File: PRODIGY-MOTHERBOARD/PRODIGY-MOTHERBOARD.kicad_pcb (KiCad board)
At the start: 2 copper layers, 217 parts, among them J1 USB_A, J10 CAN, J11 SERIAL, J12 MOTOR, J13 MOTOR, J15 Barrel_Jack_MountingPin, J16 AudioJack3, J19 KEYPAD_MATRIX, J2 SERVO, J20 Ultrasonic, J21 GPIO, J22 GPIO, J23 GPIO, J24 12V OUT, J3 SERVO, J4 SERVO, J5 GPIO, J6 DM3BT-DSF-PEJS/C, J7 A_OUT, J8 SPI_OUT, J9 I2C, P2 USB_C_Plug, Q1 BC850, Q2 BS870, Q3 BC850, Q4 DMP2045U-7, Q5 BC850, SW1 SW_SPST, SW2 SW_SPST, SW3 SW_SPST, SW4 SW_SPST, U1 PN5321A3HN_C1xx, U10 DRV8870DDA, U11 CR2013-MI2120, U12 PCF8574, U13 SN74LVC1T45DBV, U15 CC56-12YWA, U16 LM386, U17 TXS0108EPW, U18 PCA9306DC, U19 PCF8574, U2 SN74LVC1T45DBV, U20 LIS2DH12TR, U21 DRV8870DDA, U22 IP4252CZ16, U23 MCP6021RT-E/OT, U24 TSDP341xx, U3 TPS22810DRV, U4 TPS54331DR, U5 TPS54331DR, U6 Si4460, U7 LM386, U8 HDC1080, U9 SN65HVD232

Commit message: CAN schematic done
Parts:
- removed C1: 4.7uF, Capacitor_SMD:C_1206_3216Metric
- removed C32: 1uF, Capacitor_SMD:C_0603_1608Metric
- removed C33: 100nF, Capacitor_SMD:C_0603_1608Metric
- removed C34: 100nF C0G, Capacitor_SMD:C_1206_3216Metric
- removed C35: 47uF, Capacitor_SMD:C_1210_3225Metric
- removed C36, C38: 10uF, Capacitor_SMD:C_1206_3216Metric
- removed the D1 at (41.6, 119.7)
- removed the D1 at (117.3, 125.7)
- removed the D10 at (19.0, 134.4)
- removed the D10 at (158.5, 135.4)
- removed the D11 at (158.5, 142.0)
- removed the D11 at (19.0, 141.0)
- removed the D12 at (33.5, 121.7)
- removed the D12 at (166.9, 115.5)
- removed the D13 at (33.5, 129.2)
- removed the D13 at (166.9, 122.2)
- removed the D14 at (166.9, 128.8)
- removed the D14 at (19.0, 147.7)
- removed the D15 at (173.6, 116.0)
- removed the D15 at (27.4, 121.2)
- removed the D16 at (27.4, 127.8)
- removed the D16 at (181.1, 116.0)
- removed the D17 at (188.6, 116.0)
- removed the D17 at (27.4, 134.4)
- removed the D2 at (17.2, 114.1)
- removed the D2 at (117.3, 136.8)
- removed the D21 at (153.7, 55.5)
- removed the D21 at (173.0, 131.1)
- removed D25, D27: SD05_SOD323, Diode_SMD:D_SOD-323
- removed the D3 at (24.7, 114.1)
- removed the D3 at (117.3, 131.2)
- removed the D4 at (32.2, 114.1)
- removed the D4 at (139.5, 84.0)
- removed the D5 at (102.5, 56.9)
- removed the D5 at (19.0, 121.2)
- removed the D6 at (181.1, 129.1)
- removed the D6 at (39.7, 114.1)
- removed the D7 at (158.5, 115.5)
- removed the D7 at (47.2, 114.1)
- removed the D8 at (54.7, 114.1)
- removed the D8 at (158.5, 122.2)
- removed the D9 at (19.0, 127.8)
- removed the D9 at (158.5, 128.8)
- removed J1: USB_A, Connector_USB:USB_A_TE_292303-7_Horizontal
- removed the J12 at (126.2, 51.8)
- removed the J12 at (89.2, 83.5)
- removed J2, J3: SERVO, Connector_JST:JST_XH_S3B-XH-A_1x03_P2.50mm_Horizontal
- removed the J4 at (169.7, 69.0)
- removed the J4 at (101.2, 70.0)
- removed P2: USB_C_Plug, Connector_USB:USB_C_Receptacle_GCT_USB4105-xx-A_16P_TopMnt_Horizontal
- removed the Q1 at (49.1, 119.7)
- removed the Q1 at (188.6, 129.1)
- removed the Q3 at (144.2, 47.0)
- removed the Q3 at (207.8, 97.1)
- removed R25: 100, Resistor_SMD:R_0805_2012Metric
- removed R26, R27, R28: 220k, Resistor_SMD:R_0805_2012Metric
- removed R29: 1k, Resistor_SMD:R_0805_2012Metric
- removed RN5: 10k, Resistor_SMD:R_Array_Convex_5x0603
- removed SW1, SW2, SW3, SW4: SW_SPST, Button_Switch_SMD:SW_SPST_EVQP0
- removed U1: PN5321A3HN_C1xx, Package_DFN_QFN:HVQFN-40-1EP_6x6mm_P0.5mm_EP4.1x4.1mm
- removed U10: DRV8870DDA, Package_SO:Texas_HTSOP-8-1EP_3.9x4.9mm_P1.27mm_EP2.95x4.9mm_Mask2.4x3.1mm_ThermalVias
- added C25: 47uF, Capacitor_SMD:C_1210_3225Metric, F.Cu at (132.8, 29.6)
- added C26: 47uF, Capacitor_SMD:C_1210_3225Metric, F.Cu at (132.8, 33.8)
- added C27: 47uF, Capacitor_SMD:C_1210_3225Metric, F.Cu at (132.8, 38.1)
- added C28: 47uF, Capacitor_SMD:CP_Elec_6.3x5.8, F.Cu at (145.0, 155.5)
- added C29: 47uF, Capacitor_SMD:CP_Elec_6.3x5.8, F.Cu at (145.0, 163.6)
- added C40: 100nF, Capacitor_SMD:C_0603_1608Metric, F.Cu at (83.2, 145.2)
- added C41: 100nF C0G, Capacitor_SMD:C_1206_3216Metric, F.Cu at (77.9, 150.6)
- added C42: 47uF, Capacitor_SMD:C_1210_3225Metric, F.Cu at (77.9, 157.8)
- added C43: 10uF, Capacitor_SMD:C_1206_3216Metric, F.Cu at (77.9, 154.0)
- added C58: 100nF, Capacitor_SMD:C_0603_1608Metric, F.Cu at (85.7, 64.5)
- added D1: D_Schottky, Diode_SMD:D_SMB, F.Cu at (148.0, 142.2)
- added D10: LED, LED_THT:LED_D5.0mm, F.Cu at (110.3, 146.2)
- added D11: LED, LED_THT:LED_D5.0mm, F.Cu at (117.8, 146.2)
- added D12: LED, LED_THT:LED_D5.0mm, F.Cu at (125.3, 146.2)
- added D13: WS2812B, LED_SMD:LED_WS2812B_PLCC4_5.0x5.0mm_P3.2mm, F.Cu at (95.2, 128.2)
- added D14: D_IR_EMITTER, LED_THT:LED_D5.0mm_Horizontal_O1.27mm_Z3.0mm_Clear, F.Cu at (126.8, 159.3)
- added D15: WS2812B, LED_SMD:LED_WS2812B_PLCC4_5.0x5.0mm_P3.2mm, F.Cu at (95.2, 134.8)
- added D16: WS2812B, LED_SMD:LED_WS2812B_PLCC4_5.0x5.0mm_P3.2mm, F.Cu at (95.2, 141.4)
- added D17: WS2812B, LED_SMD:LED_WS2812B_PLCC4_5.0x5.0mm_P3.2mm, F.Cu at (95.2, 148.0)
- added D2: SD05_SOD323, Diode_SMD:D_SOD-323, F.Cu at (154.3, 140.8)
- added D21: LED, LED_THT:LED_D5.0mm, F.Cu at (117.8, 153.8)
- added D22: WS2812B, LED_SMD:LED_WS2812B_PLCC4_5.0x5.0mm_P3.2mm, F.Cu at (103.6, 128.2)
- added D29: SD05_SOD323, Diode_SMD:D_SOD-323, F.Cu at (83.0, 71.3)
- added D3: SD05_SOD323, Diode_SMD:D_SOD-323, F.Cu at (154.3, 143.8)
- added D30: SD05_SOD323, Diode_SMD:D_SOD-323, F.Cu at (83.0, 74.2)
- added D4: D_Schottky, Diode_SMD:D_SMB, F.Cu at (161.6, 21.7)
- added D5: D_Schottky, Diode_SMD:D_SMB, F.Cu at (161.6, 27.3)
- added D6: D_Schottky, Diode_SMD:D_SMB, F.Cu at (161.6, 32.8)
- added D7: D_Schottky, Diode_SMD:D_SMB, F.Cu at (154.4, 72.8)
- added D8: SD05_SOD323, Diode_SMD:D_SOD-323, F.Cu at (82.9, 150.4)
- added D9: SD05_SOD323, Diode_SMD:D_SOD-323, F.Cu at (82.9, 153.4)
- added J12: I2C, Connector_JST:JST_XH_S4B-XH-A_1x04_P2.50mm_Horizontal, F.Cu at (22.7, 84.5)
- added J14: SERIAL, Connector_JST:JST_XH_S4B-XH-A_1x04_P2.50mm_Horizontal, F.Cu at (22.7, 111.7)
- added J17: SERVO, Connector_JST:JST_XH_S3B-XH-A_1x03_P2.50mm_Horizontal, F.Cu at (68.5, 111.7)
- added J18: SERVO, Connector_JST:JST_XH_S3B-XH-A_1x03_P2.50mm_Horizontal, F.Cu at (80.5, 111.7)
- added J26: KEYPAD_MATRIX, Connector_PinHeader_2.54mm:PinHeader_1x08_P2.54mm_Vertical_SMD_Pin1Left, F.Cu at (23.2, 68.0)
- added J4: USB_A, Connector_USB:USB_A_TE_292303-7_Horizontal, F.Cu at (62.2, 130.8)
- added L3: L_Iron_Coupled_1324, Inductor_SMD:L_CommonModeChoke_TDK_ACM7060, F.Cu at (92.0, 72.5)
- added P1: USB_C_Plug, Connector_USB:USB_C_Receptacle_GCT_USB4105-xx-A_16P_TopMnt_Horizontal, F.Cu at (156.1, 65.3)
- added Q1: DMP2045U-7, Package_TO_SOT_SMD:SOT-23, F.Cu at (65.5, 159.6)
- added Q3: BC850, Package_TO_SOT_SMD:SOT-23, F.Cu at (126.3, 127.3)
- added R18: 1k 1%, Resistor_SMD:R_0603_1608Metric, F.Cu at (145.7, 35.3)
- added R19: 10k 1%, Resistor_SMD:R_0603_1608Metric, F.Cu at (149.7, 20.2)
- added R20: 1k 1%, Resistor_SMD:R_0603_1608Metric, F.Cu at (149.7, 22.7)
- added R21: 680 1%, Resistor_SMD:R_0603_1608Metric, F.Cu at (149.7, 25.2)
- added R63: 100, Resistor_SMD:R_0603_1608Metric, F.Cu at (121.8, 133.7)
- added R64: R_Photo, OptoDevice:R_LDR_5.1x4.3mm_P3.4mm_Vertical, F.Cu at (37.4, 160.8)
- added R65: 10k, Resistor_SMD:R_0603_1608Metric, F.Cu at (91.7, 64.5)
- added R66: 100, Resistor_SMD:R_0603_1608Metric, F.Cu at (91.7, 67.0)
- added R67: 59, Resistor_SMD:R_1206_3216Metric, F.Cu at (78.0, 71.5)
- added R68: 59, Resistor_SMD:R_1206_3216Metric, F.Cu at (78.0, 74.8)
- added RN4: 4.7k, Resistor_SMD:R_Array_Convex_4x0603, F.Cu at (33.4, 67.5)
- added U14: SN74LVC1T45DBV, Package_TO_SOT_SMD:SOT-23-6, F.Cu at (164.5, 97.5)
- added U25: TJA1051T-E, Package_SO:SOIC-8_3.9x4.9mm_P1.27mm, F.Cu at (79.4, 66.6)
- C10: value 100nF -> 4.7uF; footprint Capacitor_SMD:C_0603_1608Metric -> Capacitor_SMD:C_1206_3216Metric
- C11, C12: value 10nF -> 4.7uF; footprint Capacitor_SMD:C_0603_1608Metric -> Capacitor_SMD:C_1206_3216Metric
- C13: value 1nF -> 4.7uF; footprint Capacitor_SMD:C_0603_1608Metric -> Capacitor_SMD:C_1206_3216Metric
- C14: value 4.7nF -> 100nF
- C15: value 47pF -> 100nF
- C16: value 39pF -> 10nF
- C17: value 100nF -> 10nF
- C18: value 100nF -> 1nF
- C19: value 47uF -> 4.7nF; footprint Capacitor_SMD:C_1210_3225Metric -> Capacitor_SMD:C_0603_1608Metric
- C2: value 22nF -> 10uF; footprint Capacitor_SMD:C_0603_1608Metric -> Capacitor_SMD:C_0805_2012Metric
- C20: value 47uF -> 47pF; footprint Capacitor_SMD:C_1210_3225Metric -> Capacitor_SMD:C_0603_1608Metric
- C21: value 47uF -> 39pF; footprint Capacitor_SMD:C_1210_3225Metric -> Capacitor_SMD:C_0603_1608Metric
- C22: value 47uF -> 100nF; footprint Capacitor_SMD:C_1210_3225Metric -> Capacitor_SMD:C_0603_1608Metric
- C23: value 10uF -> 100nF; footprint Capacitor_SMD:C_0805_2012Metric -> Capacitor_SMD:C_0603_1608Metric
- C24, C9: value 100nF -> 47uF; footprint Capacitor_SMD:C_0603_1608Metric -> Capacitor_SMD:C_1210_3225Metric
- C3: value 100uF -> 100nF; footprint Capacitor_SMD:CP_Elec_6.3x7.7 -> Capacitor_SMD:C_0603_1608Metric
- C39: value 100nF -> 1uF; footprint Capacitor_SMD:C_0805_2012Metric -> Capacitor_SMD:C_0603_1608Metric
- C4: value 47uF -> 10uF; footprint Capacitor_SMD:C_1210_3225Metric -> Capacitor_SMD:C_1206_3216Metric
- C5: value 4.7uF -> 100nF; footprint Capacitor_SMD:C_1206_3216Metric -> Capacitor_SMD:C_0805_2012Metric
- C7: value 4.7uF -> 22nF; footprint Capacitor_SMD:C_1206_3216Metric -> Capacitor_SMD:C_0603_1608Metric
- C8: value 4.7uF -> 100uF; footprint Capacitor_SMD:C_1206_3216Metric -> Capacitor_SMD:CP_Elec_6.3x7.7
- D18, D23: value LED -> WS2812B; footprint LED_THT:LED_D5.0mm -> LED_SMD:LED_WS2812B_PLCC4_5.0x5.0mm_P3.2mm
- D24: value SD05_SOD323 -> WS2812B; footprint Diode_SMD:D_SOD-323 -> LED_SMD:LED_WS2812B_PLCC4_5.0x5.0mm_P3.2mm
- D26: value SD05_SOD323 -> LED; footprint Diode_SMD:D_SOD-323 -> LED_THT:LED_D5.0mm
- J10: value CAN -> GPIO; footprint Connector_JST:JST_XH_S4B-XH-A_1x04_P2.50mm_Horizontal -> Connector_JST:JST_XH_S3B-XH-A_1x03_P2.50mm_Horizontal
- J11: value SERIAL -> SPI_OUT; footprint Connector_JST:JST_XH_S4B-XH-A_1x04_P2.50mm_Horizontal -> Connector_JST:JST_XH_S6B-XH-A_1x06_P2.50mm_Horizontal
- J13: value MOTOR -> CAN; footprint Connector_JST:JST_XH_S6B-XH-A_1x06_P2.50mm_Horizontal -> Connector_JST:JST_XH_S4B-XH-A_1x04_P2.50mm_Horizontal
- J15: value Barrel_Jack_MountingPin -> 12V OUT; footprint Connector_BarrelJack:BarrelJack_CUI_PJ-063AH_Horizontal -> TerminalBlock_Phoenix:TerminalBlock_Phoenix_MKDS-1,5-2-5.08_1x02_P5.08mm_Horizontal
- J16: value AudioJack3 -> SERVO; footprint Connector_Audio:Jack_3.5mm_Lumberg_1503_07_Horizontal -> Connector_JST:JST_XH_S3B-XH-A_1x03_P2.50mm_Horizontal
- J19: value KEYPAD_MATRIX -> Ultrasonic; footprint Connector_PinHeader_2.54mm:PinHeader_1x08_P2.54mm_Vertical_SMD_Pin1Left -> Connector_JST:JST_XH_S4B-XH-A_1x04_P2.50mm_Horizontal
- J20: value Ultrasonic -> MOTOR; footprint Connector_JST:JST_XH_S4B-XH-A_1x04_P2.50mm_Horizontal -> Connector_JST:JST_XH_S6B-XH-A_1x06_P2.50mm_Horizontal
- J21: value GPIO -> MOTOR; footprint Connector_JST:JST_XH_S3B-XH-A_1x03_P2.50mm_Horizontal -> Connector_JST:JST_XH_S6B-XH-A_1x06_P2.50mm_Horizontal
- J22: value GPIO -> DM3BT-DSF-PEJS/C; footprint Connector_JST:JST_XH_S3B-XH-A_1x03_P2.50mm_Horizontal -> Connector_Card:microSD_HC_Hirose_DM3BT-DSF-PEJS
- J23: value GPIO -> Barrel_Jack_MountingPin; footprint Connector_JST:JST_XH_S3B-XH-A_1x03_P2.50mm_Horizontal -> Connector_BarrelJack:BarrelJack_CUI_PJ-063AH_Horizontal
- J24: value 12V OUT -> AudioJack3; footprint TerminalBlock_Phoenix:TerminalBlock_Phoenix_MKDS-1,5-2-5.08_1x02_P5.08mm_Horizontal -> Connector_Audio:Jack_3.5mm_Lumberg_1503_07_Horizontal
- J5: value GPIO -> A_OUT
- J6: value DM3BT-DSF-PEJS/C -> Neopixel; footprint Connector_Card:microSD_HC_Hirose_DM3BT-DSF-PEJS -> Connector_JST:JST_XH_S3B-XH-A_1x03_P2.50mm_Horizontal
- J7: value A_OUT -> GPIO
- J8: value SPI_OUT -> GPIO; footprint Connector_JST:JST_XH_S6B-XH-A_1x06_P2.50mm_Horizontal -> Connector_JST:JST_XH_S3B-XH-A_1x03_P2.50mm_Horizontal
- J9: value I2C -> GPIO; footprint Connector_JST:JST_XH_S4B-XH-A_1x04_P2.50mm_Horizontal -> Connector_JST:JST_XH_S3B-XH-A_1x03_P2.50mm_Horizontal
- Q2: value BS870 -> BC850
- Q4: value DMP2045U-7 -> BS870
- R1: value DNP -> 10k
- R10, R12: value 1k 1% -> 330k
- R11: value 10k 1% -> 68k
- R13: value 680 1% -> 68k
- R14: value 220 1% -> 29.4k
- R15: value R_Photo -> 50k; footprint OptoDevice:R_LDR_5.1x4.3mm_P3.4mm_Vertical -> Resistor_SMD:R_0603_1608Metric
- R16: value 33k -> 10k 1%
- R17: value 10k -> 2.2k 1%
- R2: value 330k -> 100
- R22: value 1k -> 220 1%; footprint Resistor_SMD:R_0805_2012Metric -> Resistor_SMD:R_0603_1608Metric
- R23: value 1k -> 2; footprint Resistor_SMD:R_0805_2012Metric -> Resistor_SMD:R_2512_6332Metric
- R24: value 68k -> 2; footprint Resistor_SMD:R_0805_2012Metric -> Resistor_SMD:R_2512_6332Metric
- R3: value 68k -> 5.1k
- R30, R37: value 10k -> 1k; footprint Resistor_SMD:R_0603_1608Metric -> Resistor_SMD:R_0805_2012Metric
- R31: value 100 -> 1k; footprint Resistor_SMD:R_0603_1608Metric -> Resistor_SMD:R_0805_2012Metric
- R32: value 10k -> 68k; footprint Resistor_SMD:R_0603_1608Metric -> Resistor_SMD:R_0805_2012Metric
- R33: value 10k -> 100; footprint Resistor_SMD:R_0603_1608Metric -> Resistor_SMD:R_0805_2012Metric
- R34, R36: value 100 -> 220k; footprint Resistor_SMD:R_0603_1608Metric -> Resistor_SMD:R_0805_2012Metric
- R35: value 10k -> 220k; footprint Resistor_SMD:R_0603_1608Metric -> Resistor_SMD:R_0805_2012Metric
- R38, R40, R58: value 100 -> 1k
- R39: value 10k -> 1k
- R4: value 330k -> 5.1k
- R41, R62: value 10k -> 100
- R42: value 100 -> 39
- R43, R44: value 5.1k -> 1k
- R46, R51, R53, R54: value 1k -> 10k
- R47, R55, R56: value 1k -> 100
- R5: value 68k -> 33k
- R52: value 1k -> 22; footprint Resistor_SMD:R_0603_1608Metric -> Resistor_SMD:R_2512_6332Metric
- R57: value 39 -> 1k
- R59: value DNP -> 1k; footprint Resistor_SMD:R_2512_6332Metric -> Resistor_SMD:R_0603_1608Metric
- R6: value 29.4k -> 10k
- R61: value 100 -> 10k
- R7: value 50k -> 10k
- R8: value 10k 1% -> 100
- R9: value 2.2k 1% -> DNP
- RN1: value 4.7k -> 10k; footprint Resistor_SMD:R_Array_Convex_4x0603 -> Resistor_SMD:R_Array_Convex_5x0603
- RV1: value R_Potentiometer -> 10k; footprint Potentiometer_THT:Potentiometer_Piher_PT-15-V15_Vertical -> Potentiometer_SMD:Potentiometer_Bourns_3224J_Horizontal
- RV2: value 10k -> 2k; footprint Potentiometer_SMD:Potentiometer_Bourns_3224J_Horizontal -> Potentiometer_SMD:Potentiometer_Bourns_3314J_Vertical
- RV3: value 2k -> R_Potentiometer; footprint Potentiometer_SMD:Potentiometer_Bourns_3314J_Vertical -> Potentiometer_THT:Potentiometer_Piher_PT-15-V15_Vertical
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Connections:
- C10 pad 1: +5V -> +12V
- C11 pad 1: Net-(U4-SS) -> +5V
- C12 pad 1: Net-(U5-SS) -> +12V
- C13 pad 1: Net-(U4-COMP) -> +5V
- C13 pad 2: Net-(C13-Pad2) -> GND
- C14 pad 1: Net-(U5-COMP) -> +12V
- C14 pad 2: Net-(C14-Pad2) -> GND
- C15 pad 1: Net-(U4-COMP) -> +5V
- C16 pad 1: Net-(U5-COMP) -> Net-(U6-SS)
- C17 pad 1: Net-(U4-BOOT) -> Net-(U7-SS)
- C17 pad 2: Net-(D2-K) -> GND
- C18 pad 1: Net-(U5-BOOT) -> Net-(U6-COMP)
- C18 pad 2: Net-(D3-K) -> Net-(C18-Pad2)
- C19 pad 1: /POWER/+3V3 -> Net-(U7-COMP)
- C19 pad 2: GND -> Net-(C19-Pad2)
- C2 pad 1: Net-(U3-CT) -> +5V
- C20 pad 1: +5V -> Net-(U6-COMP)
- C21 pad 1: /POWER/+3V3 -> Net-(U7-COMP)
- C22 pad 1: +5V -> Net-(U6-BOOT)
- C22 pad 2: GND -> Net-(D5-K)
- C23 pad 1: +5V -> Net-(U7-BOOT)
- C23 pad 2: GND -> Net-(D6-K)
- C24 pad 1: +5V -> /POWER/+3V3
- C3 pad 1: +12V -> +5V
- C39 pad 1: /SPI/micro_SD/SD_VCC -> /50Hz Filter/3.3VA_1
- C4 pad 1: /OUTPUTS/BREAKOUT_USB_VBUS -> /SPI/micro_SD/SD_VCC
- C5 pad 1: +12V -> /SPI/micro_SD/SD_VCC
- C7 pad 1: +12V -> Net-(U5-CT)
- C8 pad 1: +5V -> +12V
- C9 pad 1: +12V -> /OUTPUTS/BREAKOUT_USB_VBUS
- D18 pad 1: Net-(D18-K) -> +5V
- D18 pad 2: /digital/DIGITAL_LED_0 -> Net-(D18-DOUT)
- D19 pad 2: /digital/DIGITAL_LED_1 -> /digital/DIGITAL_LED_0
- D20 pad 2: /digital/DIGITAL_LED_2 -> /digital/DIGITAL_LED_1
- D23 pad 1: Net-(D23-K) -> +5V
- D23 pad 2: Net-(D23-A) -> Net-(D23-DOUT)
- D24 pad 1: GND -> +5V
- D24 pad 2: /50Hz Filter/IN_P1- -> Net-(D13-DIN)
- D26 pad 1: GND -> Net-(D26-K)
- D26 pad 2: Net-(D26-A2) -> Net-(D26-A)
- J10 pad 1: /OUTPUTS/BREAKOUT_CAN_TX -> /OUTPUTS/BREAKOUT_D_GPIO_3
- J10 pad 2: /OUTPUTS/BREAKOUT_CAN_RX -> /OUTPUTS/BREAKOUT_VCC
- J10 pad 3: /OUTPUTS/BREAKOUT_VCC -> GND
- J11 pad 1: /OUTPUTS/BREAKOUT_SERIAL_TX -> /SPI/CS_BREAKOUT
- J11 pad 2: /OUTPUTS/BREAKOUT_SERIAL_RX -> /SPI/CLK
- J11 pad 3: /OUTPUTS/BREAKOUT_VCC -> /SPI/MISO
- J11 pad 4: GND -> /SPI/MOSI
- J13 pad 1: /OUTPUTS/BREAKOUT_MOTOR_PWM1_2 -> /CAN/CAN_H
- J13 pad 2: /OUTPUTS/BREAKOUT_MOTOR_PWM2_2 -> /CAN/CAN_L
- J13 pad 3: /OUTPUTS/BREAKOUT_MOTOR_C1_2 -> /OUTPUTS/BREAKOUT_VCC
- J13 pad 4: /OUTPUTS/BREAKOUT_MOTOR_C2_2 -> GND
- J15 pad 1: GND -> +12V
- J15 pad 2: Net-(F1-Pad1) -> GND
- J19 pad 1: Net-(J19-Pin_1) -> /OUTPUTS/BREAKOUT_ULTRASONIC_TRIG
- J19 pad 2: Net-(J19-Pin_2) -> /OUTPUTS/BREAKOUT_ULTRASONIC_ECHO
- J19 pad 3: Net-(J19-Pin_3) -> /OUTPUTS/BREAKOUT_VCC
- J19 pad 4: Net-(J19-Pin_4) -> GND
- J20 pad 1: /OUTPUTS/BREAKOUT_ULTRASONIC_TRIG -> /MOTOR/MOTOR_OUT1_BREAKOUT_1
- J20 pad 2: /OUTPUTS/BREAKOUT_ULTRASONIC_ECHO -> /MOTOR/MOTOR_OUT1_BREAKOUT_2
- J20 pad 3: /OUTPUTS/BREAKOUT_VCC -> /OUTPUTS/BREAKOUT_MOTOR_C1_1
- J20 pad 4: GND -> /OUTPUTS/BREAKOUT_MOTOR_C2_1
- J21 pad 1: /OUTPUTS/BREAKOUT_D_GPIO_1 -> /MOTOR/MOTOR_OUT2_BREAKOUT_1
- J21 pad 2: /OUTPUTS/BREAKOUT_VCC -> /MOTOR/MOTOR_OUT2_BREAKOUT_2
- J21 pad 3: GND -> /OUTPUTS/BREAKOUT_MOTOR_C1_2
- J22 pad 1: /OUTPUTS/BREAKOUT_D_GPIO_2 -> unconnected-(J22-DAT2-Pad1)
- J22 pad 2: /OUTPUTS/BREAKOUT_VCC -> /SPI/micro_SD/SD_CS-CS
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
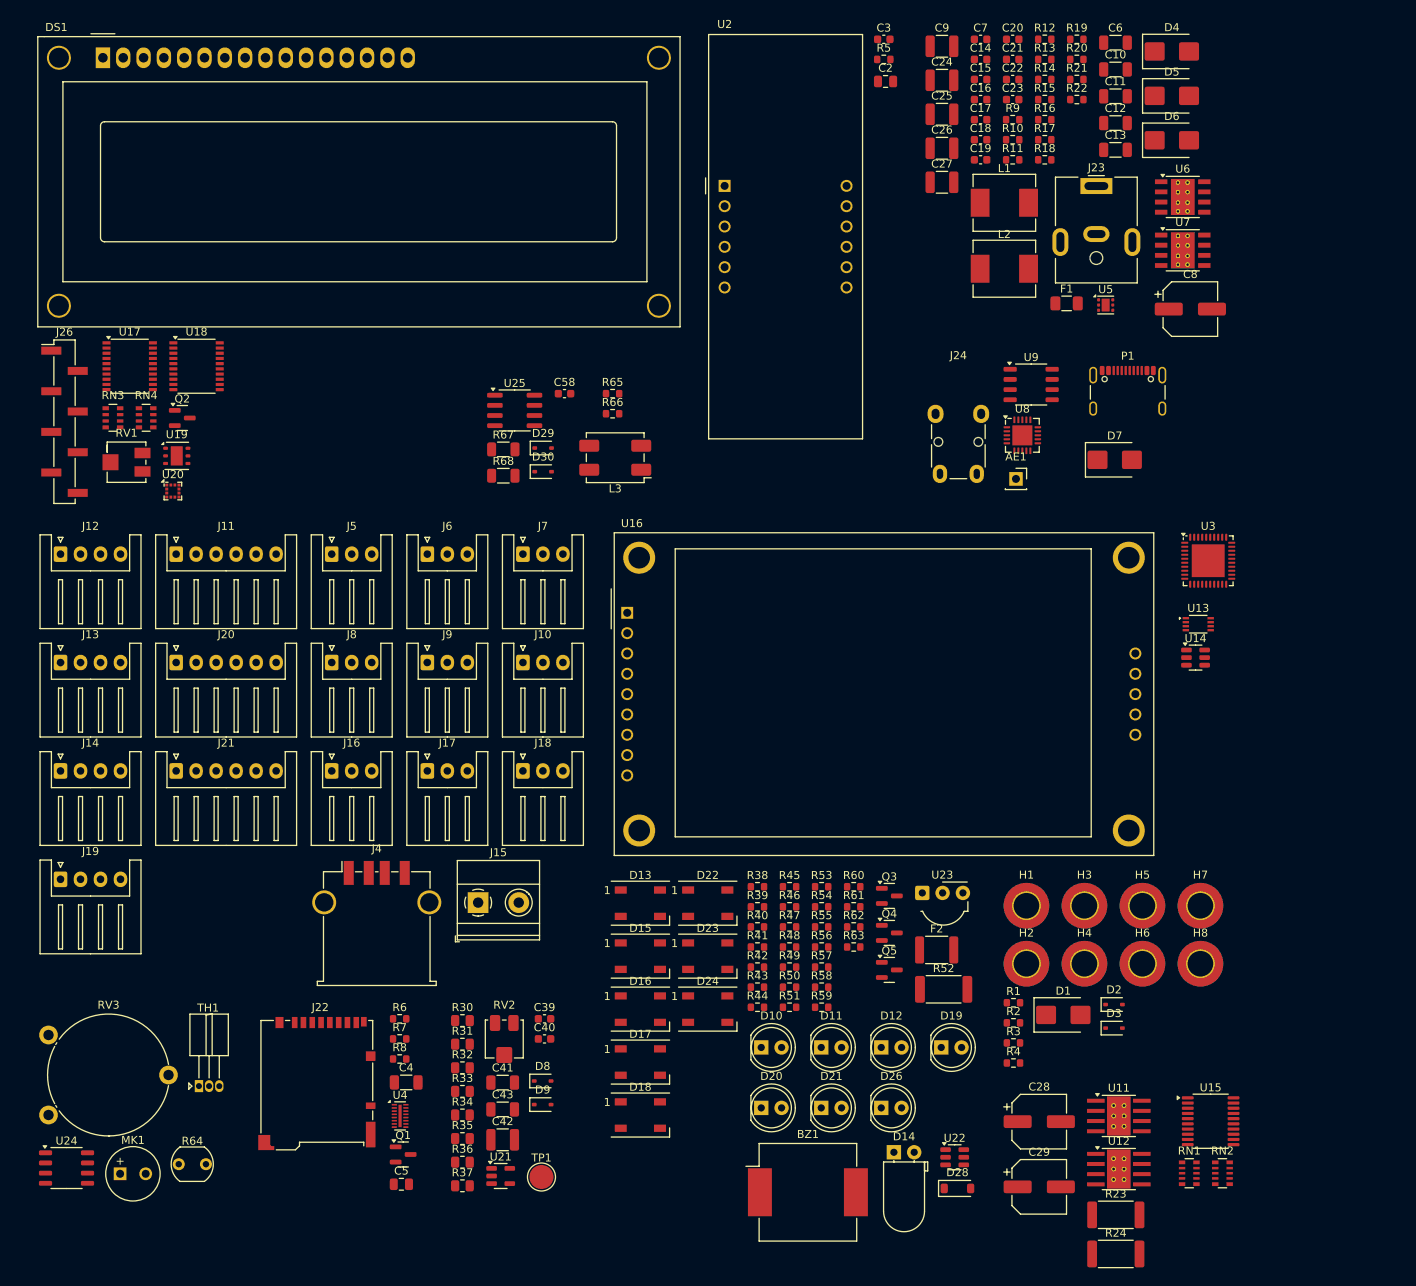
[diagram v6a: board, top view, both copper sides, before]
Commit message: Analog schematic finished, except the joystick part.
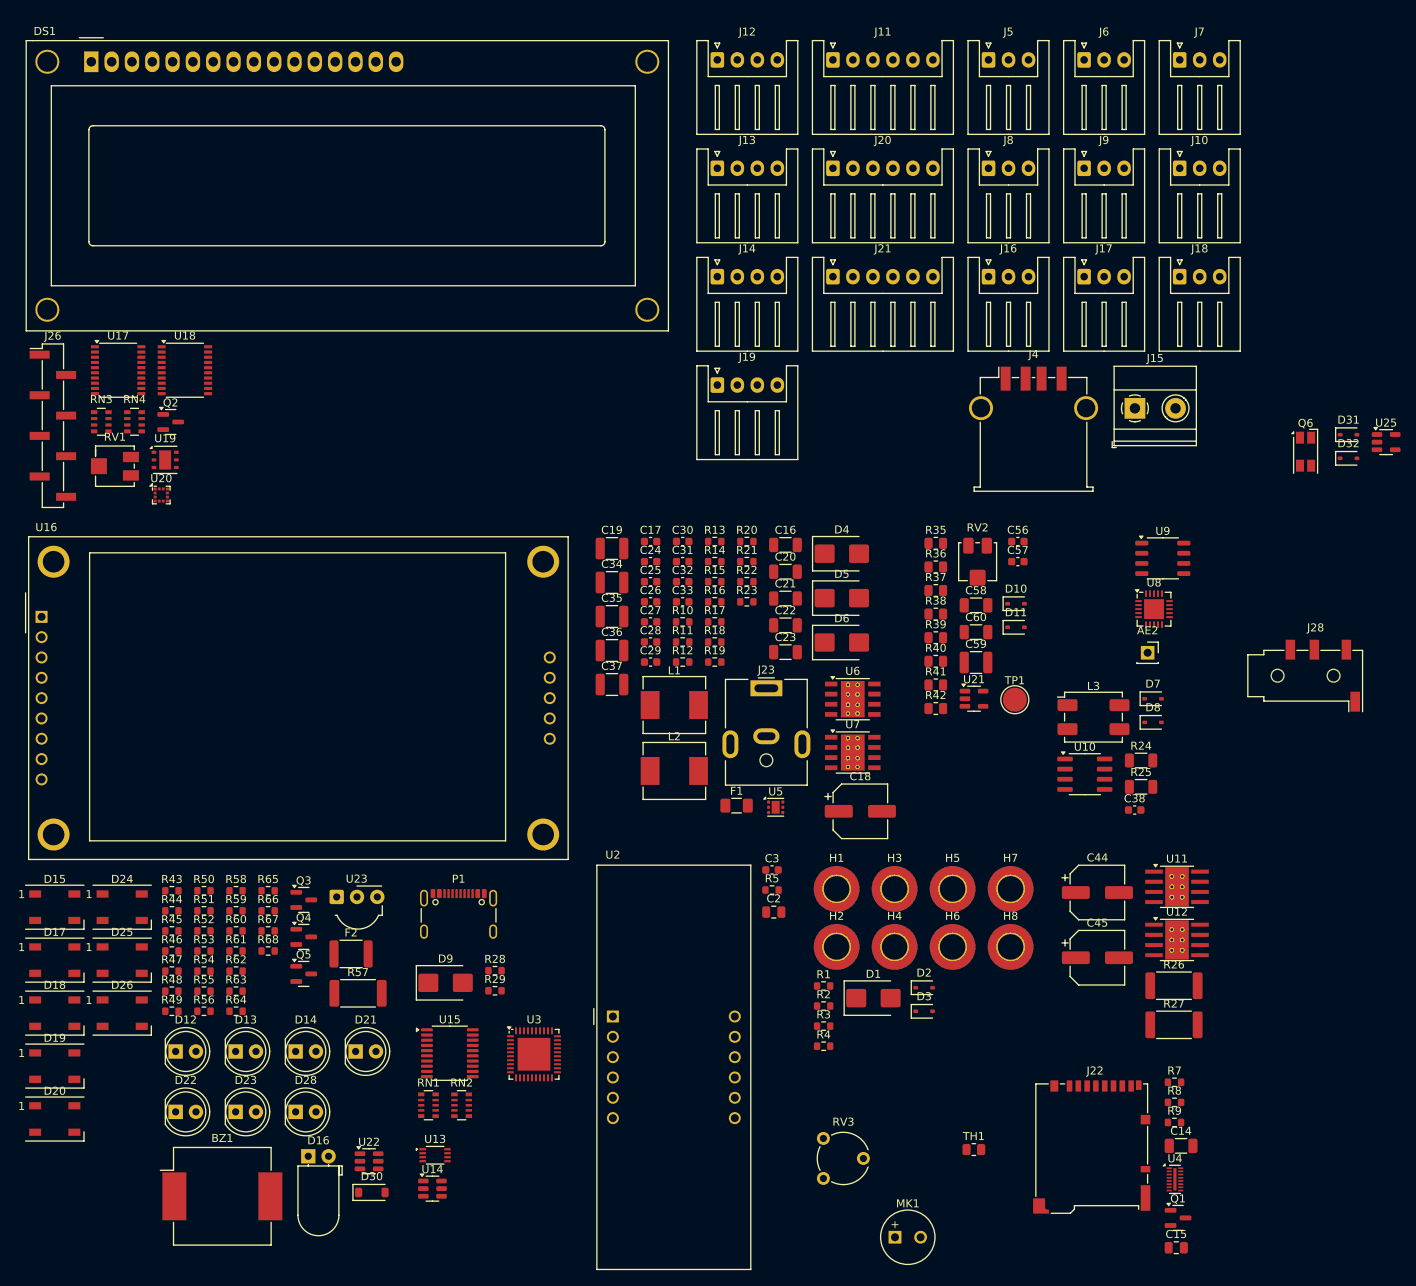
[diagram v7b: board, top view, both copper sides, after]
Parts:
- removed AE1: Antenna, Connector_PinSocket_2.54mm:PinSocket_1x01_P2.54mm_Vertical
- removed C10, C11, C12, C13, C6: 4.7uF, Capacitor_SMD:C_1206_3216Metric
- removed C39: 1uF, Capacitor_SMD:C_0603_1608Metric
- removed C4, C43: 10uF, Capacitor_SMD:C_1206_3216Metric
- removed C40: 100nF, Capacitor_SMD:C_0603_1608Metric
- removed C41: 100nF C0G, Capacitor_SMD:C_1206_3216Metric
- removed C42, C9: 47uF, Capacitor_SMD:C_1210_3225Metric
- removed C5: 100nF, Capacitor_SMD:C_0805_2012Metric
- removed C7: 22nF, Capacitor_SMD:C_0603_1608Metric
- removed C8: 100uF, Capacitor_SMD:CP_Elec_6.3x7.7
- removed D29: SD05_SOD323, Diode_SMD:D_SOD-323
- removed J24: AudioJack3, Connector_Audio:Jack_3.5mm_Lumberg_1503_07_Horizontal
- removed R30, R31: 1k, Resistor_SMD:R_0805_2012Metric
- removed R32: 68k, Resistor_SMD:R_0805_2012Metric
- removed R33: 100, Resistor_SMD:R_0805_2012Metric
- removed R34: 220k, Resistor_SMD:R_0805_2012Metric
- removed R6: 10k, Resistor_SMD:R_0603_1608Metric
- removed U24: LM386, Package_SO:SOP-8_3.9x4.9mm_P1.27mm
- added AE2: Antenna, Connector_PinSocket_2.54mm:PinSocket_1x01_P2.54mm_Vertical, F.Cu at (158.6, 96.9)
- added C30: 47pF, Capacitor_SMD:C_0603_1608Metric, F.Cu at (100.4, 83.0)
- added C31: 39pF, Capacitor_SMD:C_0603_1608Metric, F.Cu at (100.4, 85.5)
- added C32: 100nF, Capacitor_SMD:C_0603_1608Metric, F.Cu at (100.4, 88.0)
- added C33: 100nF, Capacitor_SMD:C_0603_1608Metric, F.Cu at (100.4, 90.5)
- added C34: 47uF, Capacitor_SMD:C_1210_3225Metric, F.Cu at (91.6, 88.1)
- added C35: 47uF, Capacitor_SMD:C_1210_3225Metric, F.Cu at (91.6, 92.3)
- added C36: 47uF, Capacitor_SMD:C_1210_3225Metric, F.Cu at (91.6, 96.6)
- added C37: 47uF, Capacitor_SMD:C_1210_3225Metric, F.Cu at (91.6, 100.8)
- added C38: 100nF, Capacitor_SMD:C_0603_1608Metric, F.Cu at (156.9, 116.5)
- added C44: 47uF, Capacitor_SMD:CP_Elec_6.3x5.8, F.Cu at (152.3, 126.8)
- added C45: 47uF, Capacitor_SMD:CP_Elec_6.3x5.8, F.Cu at (152.3, 135.0)
- added C56: 1uF, Capacitor_SMD:C_0603_1608Metric, F.Cu at (142.3, 83.0)
- added C57: 100nF, Capacitor_SMD:C_0603_1608Metric, F.Cu at (142.3, 85.5)
- added C59: 47uF, Capacitor_SMD:C_1210_3225Metric, F.Cu at (137.1, 98.1)
- added C60: 10uF, Capacitor_SMD:C_1206_3216Metric, F.Cu at (137.1, 94.3)
- added D25: WS2812B, LED_SMD:LED_WS2812B_PLCC4_5.0x5.0mm_P3.2mm, F.Cu at (30.4, 135.3)
- added D31: SD05_SOD323, Diode_SMD:D_SOD-323, F.Cu at (183.7, 69.6)
- added D32: SD05_SOD323, Diode_SMD:D_SOD-323, F.Cu at (183.7, 72.6)
- added J28: AudioJack4, Connector_Audio:Jack_3.5mm_KoreanHropartsElec_PJ-320D-4A_Horizontal, F.Cu at (179.6, 99.8)
- added Q6: ALS-PDIC15-21B/TR8, OptoDevice:Kingbright_KPS-3227, F.Cu at (178.3, 71.8)
- added R25: 59, Resistor_SMD:R_1206_3216Metric, F.Cu at (157.7, 113.6)
- added R26: 2, Resistor_SMD:R_2512_6332Metric, F.Cu at (161.8, 138.5)
- added R27: 2, Resistor_SMD:R_2512_6332Metric, F.Cu at (161.8, 143.4)
- added R28: 10k, Resistor_SMD:R_0603_1608Metric, F.Cu at (77.0, 136.6)
- added R29: 100, Resistor_SMD:R_0603_1608Metric, F.Cu at (77.0, 139.1)
- added U10: TJA1051T-E, Package_SO:SOIC-8_3.9x4.9mm_P1.27mm, F.Cu at (150.7, 112.1)
- C14: value 100nF -> 10uF; footprint Capacitor_SMD:C_0603_1608Metric -> Capacitor_SMD:C_1206_3216Metric
- C15: footprint Capacitor_SMD:C_0603_1608Metric -> Capacitor_SMD:C_0805_2012Metric
- C16: value 10nF -> 4.7uF; footprint Capacitor_SMD:C_0603_1608Metric -> Capacitor_SMD:C_1206_3216Metric
- C17: value 10nF -> 22nF
- C18: value 1nF -> 100uF; footprint Capacitor_SMD:C_0603_1608Metric -> Capacitor_SMD:CP_Elec_6.3x7.7
- C19: value 4.7nF -> 47uF; footprint Capacitor_SMD:C_0603_1608Metric -> Capacitor_SMD:C_1210_3225Metric
- C20: value 47pF -> 4.7uF; footprint Capacitor_SMD:C_0603_1608Metric -> Capacitor_SMD:C_1206_3216Metric
- C21: value 39pF -> 4.7uF; footprint Capacitor_SMD:C_0603_1608Metric -> Capacitor_SMD:C_1206_3216Metric
- C22, C23: value 100nF -> 4.7uF; footprint Capacitor_SMD:C_0603_1608Metric -> Capacitor_SMD:C_1206_3216Metric
- C24, C25: value 47uF -> 100nF; footprint Capacitor_SMD:C_1210_3225Metric -> Capacitor_SMD:C_0603_1608Metric
- C26, C27: value 47uF -> 10nF; footprint Capacitor_SMD:C_1210_3225Metric -> Capacitor_SMD:C_0603_1608Metric
- C28: value 47uF -> 1nF; footprint Capacitor_SMD:CP_Elec_6.3x5.8 -> Capacitor_SMD:C_0603_1608Metric
- C29: value 47uF -> 4.7nF; footprint Capacitor_SMD:CP_Elec_6.3x5.8 -> Capacitor_SMD:C_0603_1608Metric
- C58: value 100nF -> 100nF C0G; footprint Capacitor_SMD:C_0603_1608Metric -> Capacitor_SMD:C_1206_3216Metric
- D10, D11: value LED -> SD05_SOD323; footprint LED_THT:LED_D5.0mm -> Diode_SMD:D_SOD-323
- D13, D22, D23: value WS2812B -> LED; footprint LED_SMD:LED_WS2812B_PLCC4_5.0x5.0mm_P3.2mm -> LED_THT:LED_D5.0mm
- D14: value D_IR_EMITTER -> LED; footprint LED_THT:LED_D5.0mm_Horizontal_O1.27mm_Z3.0mm_Clear -> LED_THT:LED_D5.0mm
- D16: value WS2812B -> D_IR_EMITTER; footprint LED_SMD:LED_WS2812B_PLCC4_5.0x5.0mm_P3.2mm -> LED_THT:LED_D5.0mm_Horizontal_O1.27mm_Z3.0mm_Clear
- D19, D20, D26: value LED -> WS2812B; footprint LED_THT:LED_D5.0mm -> LED_SMD:LED_WS2812B_PLCC4_5.0x5.0mm_P3.2mm
- D28: value 1N4148W -> LED; footprint Diode_SMD:D_SOD-123 -> LED_THT:LED_D5.0mm
- D30: value SD05_SOD323 -> 1N4148W; footprint Diode_SMD:D_SOD-323 -> Diode_SMD:D_SOD-123
- D7: value D_Schottky -> SD05_SOD323; footprint Diode_SMD:D_SMB -> Diode_SMD:D_SOD-323
- D9: value SD05_SOD323 -> D_Schottky; footprint Diode_SMD:D_SOD-323 -> Diode_SMD:D_SMB
- R10: value 330k -> DNP
- R11, R13: value 68k -> 330k
- R12: value 330k -> 68k
- R14: value 29.4k -> 68k
- R15: value 50k -> 29.4k
- R16: value 10k 1% -> 50k
- R17: value 2.2k 1% -> 10k 1%
- R18: value 1k 1% -> 2.2k 1%
- R19: value 10k 1% -> 1k 1%
- R20: value 1k 1% -> 10k 1%
- R21: value 680 1% -> 1k 1%
- R22: value 220 1% -> 680 1%
- R23: value 2 -> 220 1%; footprint Resistor_SMD:R_2512_6332Metric -> Resistor_SMD:R_0603_1608Metric
- R24: value 2 -> 59; footprint Resistor_SMD:R_2512_6332Metric -> Resistor_SMD:R_1206_3216Metric
- R35, R36: value 220k -> 1k
- R37: value 1k -> 68k
- R38: value 1k -> 100; footprint Resistor_SMD:R_0603_1608Metric -> Resistor_SMD:R_0805_2012Metric
- R39, R40: value 1k -> 220k; footprint Resistor_SMD:R_0603_1608Metric -> Resistor_SMD:R_0805_2012Metric
- R41: value 100 -> 220k; footprint Resistor_SMD:R_0603_1608Metric -> Resistor_SMD:R_0805_2012Metric
- R42: value 39 -> 1k; footprint Resistor_SMD:R_0603_1608Metric -> Resistor_SMD:R_0805_2012Metric
- R46, R60, R61: value 10k -> 100
- R47: value 100 -> 39
- R52: value 22 -> 100; footprint Resistor_SMD:R_2512_6332Metric -> Resistor_SMD:R_0603_1608Metric
- R53, R54: value 10k -> 1k
- R55, R62, R63: value 100 -> 1k
- R56, R66, R8: value 100 -> 10k
- R57: value 1k -> 22; footprint Resistor_SMD:R_0603_1608Metric -> Resistor_SMD:R_2512_6332Metric
- R58, R59: value 1k -> 10k
- R64: value R_Photo -> 1k; footprint OptoDevice:R_LDR_5.1x4.3mm_P3.4mm_Vertical -> Resistor_SMD:R_0603_1608Metric
- R67, R68: value 59 -> 100; footprint Resistor_SMD:R_1206_3216Metric -> Resistor_SMD:R_0603_1608Metric
- R9: value DNP -> 100
- RV3: value R_Potentiometer -> 100k; footprint Potentiometer_THT:Potentiometer_Piher_PT-15-V15_Vertical -> Potentiometer_THT:Potentiometer_Piher_PT-6-V_Vertical
- TH1: value Thermistor -> NCT 10k; footprint Package_TO_SOT_THT:TO-92_Inline_W4.0mm_Horizontal_FlatSideUp -> Resistor_SMD:R_0805_2012Metric
- U25: value TJA1051T-E -> LMH6559; footprint Package_SO:SOIC-8_3.9x4.9mm_P1.27mm -> Package_TO_SOT_SMD:SOT-23-5
- moved C15 148.1 mm to (162.1, 171.2)
- moved C14 138.1 mm to (162.7, 158.5)
- moved R9 127.0 mm to (161.9, 155.6)
- moved U13 116.2 mm to (69.5, 159.7)
- moved U14 116.2 mm to (69.2, 163.9)
- moved D19 110.8 mm to (21.9, 148.5)
- moved U25 109.0 mm to (188.4, 70.5)
- moved P1 106.2 mm to (72.4, 130.7)
- moved C2 104.8 mm to (111.8, 129.3)
- moved R5 104.8 mm to (111.6, 126.5)
- moved C3 104.8 mm to (111.6, 124.0)
- moved U2 104.8 mm to (91.7, 142.3)
- moved U3 104.4 mm to (81.9, 147.1)
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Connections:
- net /CAN/CAN_TX renamed /analog/ANALOG_THERMISTOR_OUT
- net /SPI/CS_AUDIO renamed Net-(RN2-R7)
- net /SPI/CS_NFC renamed Net-(RN2-R5)
- net /SPI/CS_TFT renamed Net-(RN2-R6)
- C14 pad 1: +12V -> /SPI/micro_SD/SD_VCC
- C15 pad 1: +5V -> /SPI/micro_SD/SD_VCC
- C16 pad 1: Net-(U6-SS) -> +5V
- C17 pad 1: Net-(U7-SS) -> Net-(U5-CT)
- C18 pad 1: Net-(U6-COMP) -> +12V
- C18 pad 2: Net-(C18-Pad2) -> GND
- C19 pad 1: Net-(U7-COMP) -> /OUTPUTS/BREAKOUT_USB_VBUS
- C19 pad 2: Net-(C19-Pad2) -> GND
- C20 pad 1: Net-(U6-COMP) -> +12V
- C21 pad 1: Net-(U7-COMP) -> +5V
- C22 pad 1: Net-(U6-BOOT) -> +12V
- C22 pad 2: Net-(D5-K) -> GND
- C23 pad 1: Net-(U7-BOOT) -> +5V
- C23 pad 2: Net-(D6-K) -> GND
- C24 pad 1: /POWER/+3V3 -> +12V
- C26 pad 1: /POWER/+3V3 -> Net-(U6-SS)
- C27 pad 1: +5V -> Net-(U7-SS)
- C28 pad 1: +12V -> Net-(U6-COMP)
- C28 pad 2: GND -> Net-(C28-Pad2)
- C29 pad 1: +12V -> Net-(U7-COMP)
- C29 pad 2: GND -> Net-(C29-Pad2)
- C58 pad 1: +3.3V -> Net-(C58-Pad1)
- D10 pad 1: Net-(D10-K) -> GND
- D10 pad 2: /digital/DIGITAL_LED_12V -> /analog/ANALOG_POTENTIOMETER_OUT
- D11 pad 1: Net-(D11-K) -> GND
- D11 pad 2: /digital/DIGITAL_LED_5V -> +3V3
- D12 pad 2: /digital/DIGITAL_LED_3V3 -> /digital/DIGITAL_LED_12V
- D13 pad 1: +5V -> Net-(D13-K)
- D13 pad 2: Net-(D13-DOUT) -> /digital/DIGITAL_LED_5V
- D14 pad 2: Net-(D14-A) -> /digital/DIGITAL_LED_3V3
- D15 pad 4: Net-(D13-DOUT) -> Net-(D15-DIN)
- D16 pad 1: +5V -> Net-(D16-K)
- D16 pad 2: Net-(D16-DOUT) -> Net-(D16-A)
- D18 pad 4: Net-(D16-DOUT) -> Net-(D18-DIN)
- D19 pad 1: Net-(D19-K) -> +5V
- D19 pad 2: /digital/DIGITAL_LED_0 -> Net-(D19-DOUT)
- D20 pad 1: Net-(D20-K) -> +5V
- D20 pad 2: /digital/DIGITAL_LED_1 -> Net-(D20-DOUT)
- D21 pad 2: /digital/DIGITAL_LED_2 -> /digital/DIGITAL_LED_0
- D22 pad 1: +5V -> Net-(D22-K)
- D22 pad 2: /digital/DIGITAL_NEOPIXEL_OUT -> /digital/DIGITAL_LED_1
- D23 pad 1: +5V -> Net-(D23-K)
- D23 pad 2: Net-(D23-DOUT) -> /digital/DIGITAL_LED_2
- D24 pad 2: Net-(D13-DIN) -> /digital/DIGITAL_NEOPIXEL_OUT
- D24 pad 4: Net-(D23-DOUT) -> Net-(D19-DOUT)
- D26 pad 1: Net-(D26-K) -> +5V
- D26 pad 2: Net-(D26-A) -> Net-(D15-DIN)
- D28 pad 1: +3V3 -> Net-(D28-K)
- D28 pad 2: Net-(BZ1-+) -> Net-(D28-A)
- D30 pad 1: GND -> +3V3
- D30 pad 2: /CAN/CAN_L -> Net-(BZ1-+)
- D7 pad 1: +5V -> GND
- D7 pad 2: Net-(D7-A) -> /50Hz Filter/IN_P1+
- D8 pad 2: /50Hz Filter/IN_P1+ -> /50Hz Filter/IN_P1-
- D9 pad 1: GND -> +5V
- D9 pad 2: /50Hz Filter/IN_P1- -> Net-(D9-A)
- L3 pad 3: Net-(U25-CANH) -> Net-(U10-CANH)
- L3 pad 4: Net-(U25-CANL) -> Net-(U10-CANL)
- MK1 pad 1: unconnected-(MK1---Pad1) -> GND
- MK1 pad 2: unconnected-(MK1-+-Pad2) -> Net-(MK1-+)
- P1 pad A4: Net-(D7-A) -> Net-(D9-A)
- P1 pad A9: Net-(D7-A) -> Net-(D9-A)
- P1 pad B4: Net-(D7-A) -> Net-(D9-A)
- P1 pad B9: Net-(D7-A) -> Net-(D9-A)
- Q3 pad 3: Net-(D14-K) -> Net-(D16-K)
- Q4 pad 3: Net-(D26-K) -> Net-(D28-K)
- R10 pad 1: +5V -> Net-(U5-QOD)
- R10 pad 2: Net-(U6-EN) -> /OUTPUTS/BREAKOUT_USB_VBUS
- R11 pad 1: Net-(U6-EN) -> +5V
- R11 pad 2: GND -> Net-(U6-EN)
- R12 pad 1: +12V -> Net-(U6-EN)
- R12 pad 2: Net-(U7-EN) -> GND
- R13 pad 1: Net-(U7-EN) -> +12V
- R13 pad 2: GND -> Net-(U7-EN)
- R14 pad 1: Net-(C18-Pad2) -> Net-(U7-EN)
- R15 pad 1: Net-(C19-Pad2) -> Net-(C28-Pad2)
- R16 pad 1: /POWER/+3V3 -> Net-(C29-Pad2)
- R16 pad 2: Net-(U6-VSENSE) -> GND
- R17 pad 1: Net-(U6-VSENSE) -> /POWER/+3V3
- R17 pad 2: Net-(R17-Pad2) -> Net-(U6-VSENSE)
- R18 pad 1: Net-(R17-Pad2) -> Net-(U6-VSENSE)
- R18 pad 2: GND -> Net-(R18-Pad2)
- R19 pad 1: +5V -> Net-(R18-Pad2)
- R19 pad 2: Net-(U7-VSENSE) -> GND
- R20 pad 1: Net-(U7-VSENSE) -> +5V
- R20 pad 2: Net-(R20-Pad2) -> Net-(U7-VSENSE)
- R21 pad 1: Net-(R20-Pad2) -> Net-(U7-VSENSE)
- R22 pad 2: GND -> Net-(R22-Pad2)
- R23 pad 1: Net-(U11-ISEN) -> Net-(R22-Pad2)
- R24 pad 1: Net-(U12-ISEN) -> /CAN/CAN_H
- R24 pad 2: GND -> Net-(C43-Pad1)
- R35 pad 1: Net-(U21-+) -> /50Hz Filter/IN_P1+
- R35 pad 2: GND -> Net-(R35-Pad2)
- R36 pad 1: /50Hz Filter/ANALOG_BREAKOUT_IN -> /50Hz Filter/IN_P1-
- R36 pad 2: Net-(U21--) -> GND
- R37 pad 1: Net-(R37-Pad1) -> Net-(R35-Pad2)
- R38 pad 1: GND -> Net-(R35-Pad2)
- R38 pad 2: Net-(D10-K) -> Net-(C58-Pad1)
- R39 pad 1: GND -> /50Hz Filter/3.3VA_1
- R39 pad 2: Net-(D11-K) -> Net-(U21-+)
- R40 pad 1: GND -> Net-(U21-+)
- R40 pad 2: Net-(D12-K) -> GND
- R41 pad 1: /digital/DIGITAL_IR_EMITTER -> /50Hz Filter/ANALOG_BREAKOUT_OUT
- R41 pad 2: Net-(Q3-B) -> Net-(U21--)
- R42 pad 1: Net-(D14-A) -> Net-(R42-Pad1)
- R42 pad 2: +3V3 -> GND
- R43 pad 2: Net-(D19-K) -> Net-(D12-K)
- R44 pad 2: Net-(D20-K) -> Net-(D13-K)
- R45 pad 2: Net-(D21-K) -> Net-(D14-K)
- R46 pad 1: GND -> /digital/DIGITAL_IR_EMITTER
- R46 pad 2: /digital/DIGITAL_HEATER_IN -> Net-(Q3-B)
- R47 pad 1: /digital/DIGITAL_HEATER_IN -> Net-(D16-A)
- R47 pad 2: Net-(Q4-G) -> +3V3
- R48 pad 1: /digital/DIGITAL_RGB_R -> GND
- R48 pad 2: Net-(D25-RA) -> Net-(D21-K)
- R49 pad 1: /digital/DIGITAL_RGB_G -> GND
- R49 pad 2: Net-(D25-GA) -> Net-(D22-K)
- R50 pad 1: /digital/DIGITAL_RGB_B -> GND
- R50 pad 2: Net-(D25-BA) -> Net-(D23-K)
- R51 pad 1: Net-(D26-A) -> GND
- R51 pad 2: +12V -> /digital/DIGITAL_HEATER_IN
- R52 pad 1: Net-(F2-Pad2) -> /digital/DIGITAL_HEATER_IN
- R52 pad 2: Net-(D26-K) -> Net-(Q4-G)
- R53 pad 1: Net-(SW2B-D) -> /digital/DIGITAL_RGB_R
- R53 pad 2: +3V3 -> Net-(D27-RA)
- R54 pad 1: Net-(SW3A-D) -> /digital/DIGITAL_RGB_G
- R54 pad 2: +3V3 -> Net-(D27-GA)
- R55 pad 1: Net-(SW3A-D) -> /digital/DIGITAL_RGB_B
- R55 pad 2: /digital/DIGITAL_BUTTON_2 -> Net-(D27-BA)
- R56 pad 1: Net-(SW2B-D) -> Net-(D28-A)
- R56 pad 2: Net-(JP7-A) -> +12V
- R57 pad 1: /digital/DIGITAL_DETECT_R -> Net-(F2-Pad2)
- R57 pad 2: Net-(D27-RA) -> Net-(D28-K)
- R58 pad 1: /digital/DIGITAL_DETECT_G -> Net-(SW3B-D)
- R58 pad 2: Net-(D27-GA) -> +3V3
- R59 pad 1: /digital/DIGITAL_DETECT_B -> Net-(SW4A-D)
- R59 pad 2: Net-(D27-BA) -> +3V3
- R60 pad 2: +3V3 -> /digital/DIGITAL_BUTTON_2
- R61 pad 1: Net-(SW5A-D) -> Net-(SW3B-D)
- R61 pad 2: +3V3 -> Net-(JP7-A)
- R62 pad 1: Net-(SW4A-D) -> /digital/DIGITAL_DETECT_R
- R62 pad 2: /digital/DIGITAL_BUTTON_1 -> Net-(D29-RA)
- R63 pad 1: Net-(SW5A-D) -> /digital/DIGITAL_DETECT_G
- R63 pad 2: /digital/DIGITAL_BUTTON_3 -> Net-(D29-GA)
- R64 pad 1: unconnected-(R64-Pad1) -> /digital/DIGITAL_DETECT_B
- R64 pad 2: unconnected-(R64-Pad2) -> Net-(D29-BA)
- R65 pad 1: Net-(SW6A-D) -> Net-(SW5A-D)
- R66 pad 2: ESP_BUTTON_RESET -> +3V3
- R67 pad 1: /CAN/CAN_H -> Net-(SW5A-D)
- R67 pad 2: Net-(C63-Pad1) -> /digital/DIGITAL_BUTTON_1
- R68 pad 1: Net-(C63-Pad1) -> Net-(SW6A-D)
- R68 pad 2: /CAN/CAN_L -> /digital/DIGITAL_BUTTON_3
- R7 pad 1: Net-(Q1-G) -> /SPI/SPI_DETECT_SD
- R8 pad 2: /SPI/SPI_ENABLE_SD -> +3.3V
- R9 pad 1: Net-(U5-QOD) -> Net-(Q1-G)
- R9 pad 2: /OUTPUTS/BREAKOUT_USB_VBUS -> /SPI/SPI_ENABLE_SD
- RV2 pad 2: Net-(R37-Pad1) -> Net-(R42-Pad1)
- RV3 pad 1: unconnected-(RV3-Pad1) -> GND
- RV3 pad 2: unconnected-(RV3-Pad2) -> /analog/ANALOG_POTENTIOMETER_OUT
- RV3 pad 3: unconnected-(RV3-Pad3) -> +3V3
- TH1 pad 1: unconnected-(TH1-Pad1) -> +3V3
- TH1 pad 2: unconnected-(TH1-Pad2) -> Net-(D32-A2)
- TP1 pad 1: /50Hz Filter/ANALOG_BREAKOUT_IN -> /50Hz Filter/ANALOG_BREAKOUT_OUT
- U15 pad 7: /SPI/SPI_CS_NFC -> unconnected-(U15-A6-Pad7)
- U15 pad 8: /SPI/SPI_CS_TFT -> unconnected-(U15-A7-Pad8)
- U15 pad 9: /SPI/SPI_CS_AUDIO -> unconnected-(U15-A8-Pad9)
- U21 pad 1: /50Hz Filter/ANALOG_BREAKOUT_IN -> /50Hz Filter/ANALOG_BREAKOUT_OUT
- U22 pad 4: Net-(D16-DIN) -> Net-(D18-DIN)
- U25 pad 3: +3.3V -> unconnected-(U25-VREF-Pad3)
- U25 pad 4: /CAN/CAN_RX -> Net-(D32-A2)
- U25 pad 5: /CAN/CAN_EN -> +3V3
- U3 pad 1: unconnected-(U3-DVSS-Pad1) -> GND
- U3 pad 10: unconnected-(U3-RX-Pad10) -> Net-(U3-RX)
- U3 pad 11: Net-(U3-AVSS-Pad11) -> GND
- U3 pad 14: unconnected-(U3-OSCIN-Pad14) -> Net-(U3-OSCIN)
- U3 pad 15: unconnected-(U3-OSCOUT-Pad15) -> Net-(U3-OSCOUT)
- U3 pad 16: unconnected-(U3-I0-Pad16) -> +3V3
- U3 pad 17: unconnected-(U3-I1-Pad17) -> GND
- U3 pad 18: unconnected-(U3-TESTEN-Pad18) -> GND
- U3 pad 23: unconnected-(U3-PVDD-Pad23) -> +3V3
- U3 pad 27: unconnected-(U3-NSS/P50_SCL/HSU_RX-Pad27) -> /SPI/SPI_CS_NFC
- U3 pad 28: unconnected-(U3-MOSI/SDA/HSU_TX-Pad28) -> /SPI/SPI_MOSI
- U3 pad 29: unconnected-(U3-MISO/P71-Pad29) -> /SPI/SPI_MISO
- U3 pad 3: unconnected-(U3-TVSS1-Pad3) -> GND
- U3 pad 30: unconnected-(U3-SCK/P72-Pad30) -> /SPI/SPI_CLK
- U3 pad 38: unconnected-(U3-~{RSTPD}-Pad38) -> Net-(U3-~{RSTPD})
- U3 pad 39: unconnected-(U3-DVDD-Pad39) -> +3V3
- U3 pad 4: unconnected-(U3-TX1-Pad4) -> Net-(U3-TX1)
- U3 pad 40: unconnected-(U3-VBAT-Pad40) -> +3V3
- U3 pad 41: Net-(U3-AVSS-Pad11) -> GND
- U3 pad 5: unconnected-(U3-TVDD-Pad5) -> +3V3
- U3 pad 6: unconnected-(U3-TX2-Pad6) -> Net-(U3-TX2)
- U3 pad 7: unconnected-(U3-TVSS2-Pad7) -> GND
- U3 pad 8: unconnected-(U3-AVDD-Pad8) -> +3V3
- U3 pad 9: unconnected-(U3-VMID-Pad9) -> Net-(U3-VMID)
